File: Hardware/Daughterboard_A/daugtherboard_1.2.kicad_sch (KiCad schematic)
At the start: 66 parts, among them J2 RJ45, J3 RJ45, J4 Conn_01x07, J5 Conn_01x04, J6 Conn_01x07, U1 IM66D132H, U16 TXS0108EPW, U17 LP5907MFX-1.8/NOPB, U2 IM66D132H, U3 IM66D132H, U4 IM66D132H, U5 IM66D132H, U6 IM66D132H, U7 IM66D132H, U8 IM66D132H, U9 PCMD3180IRTWR

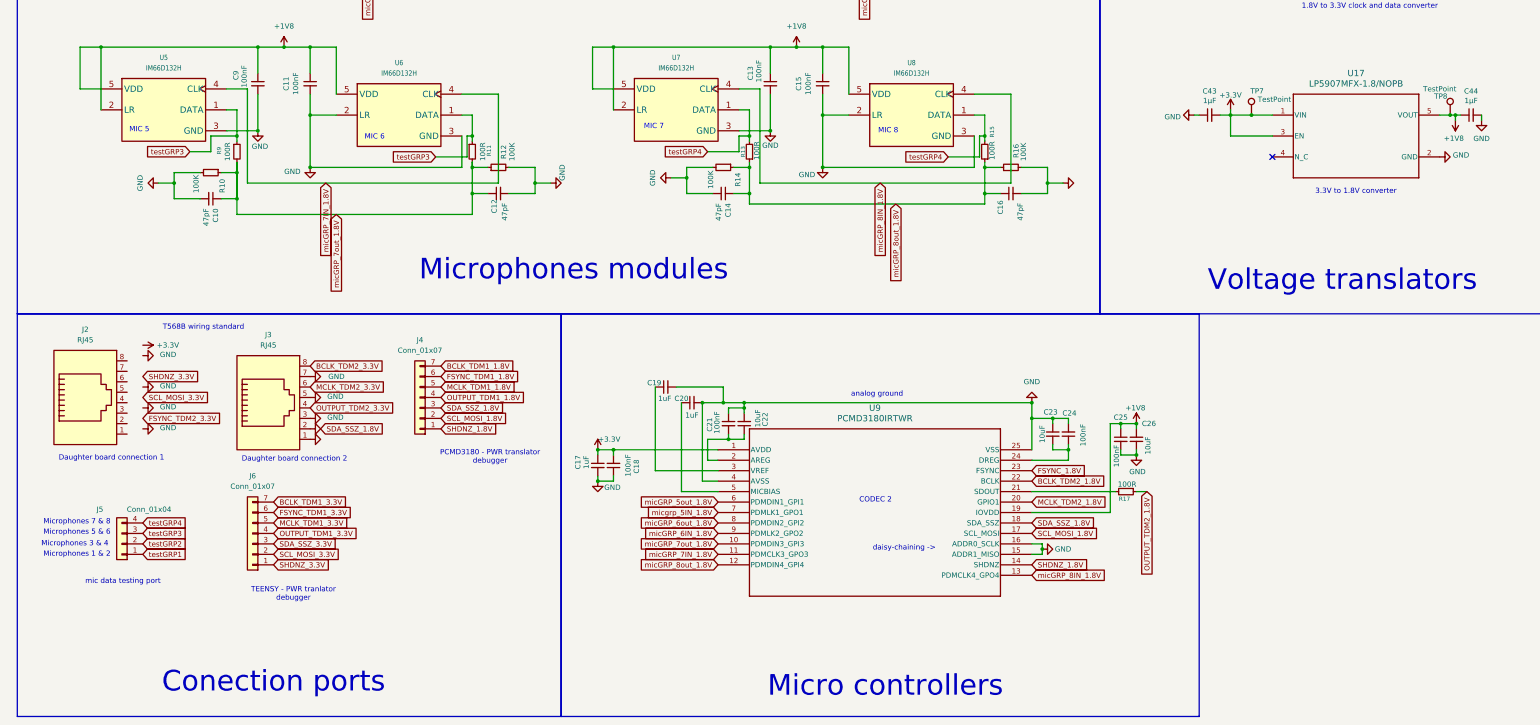
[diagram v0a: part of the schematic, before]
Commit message: ethernet port updated, fixed flaws 1.1 DB
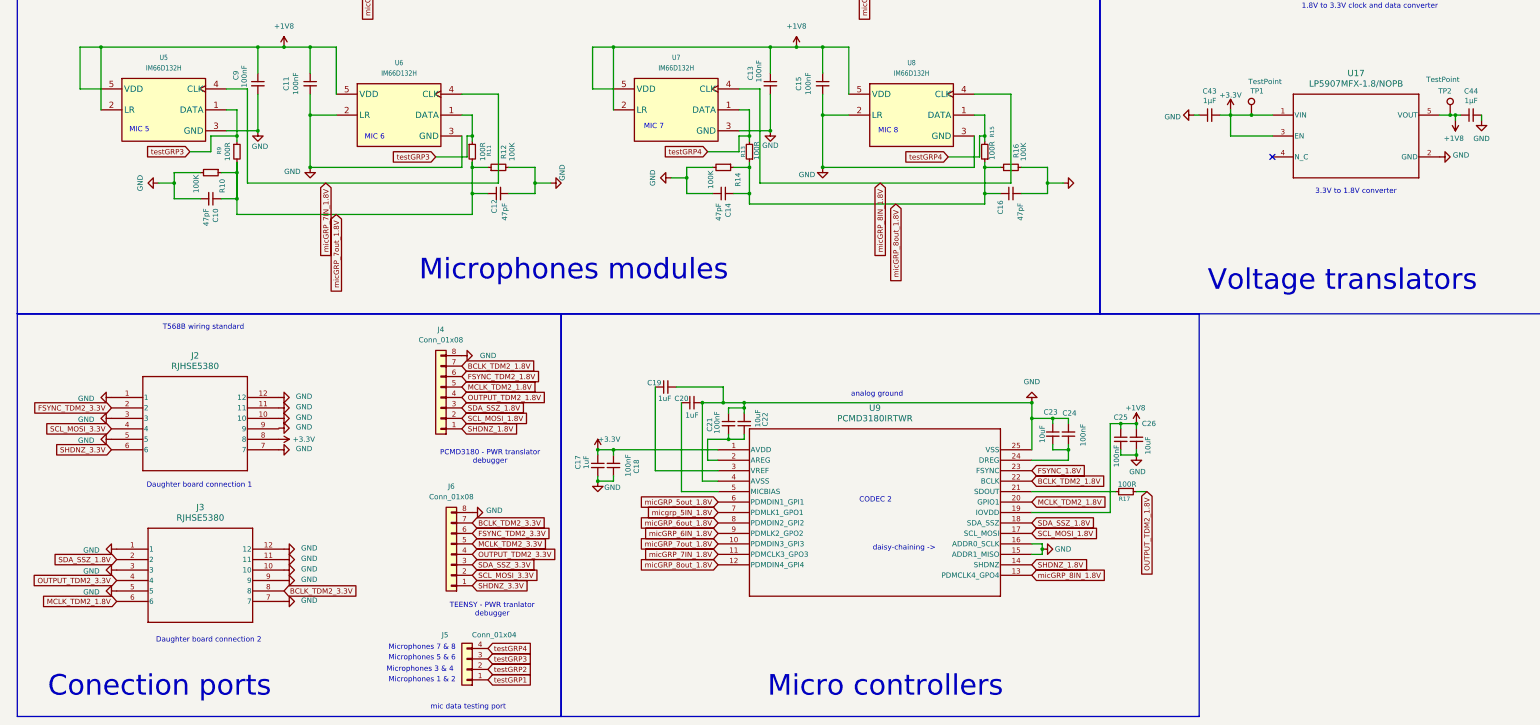
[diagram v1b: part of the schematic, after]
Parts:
- removed J2, J3: RJ45, RJHSE-3380:CONN_RJHSE-3380_AMP, symbol Connector:RJ45
- removed J4, J6: Conn_01x07, Connector_PinHeader_1.00mm:PinHeader_1x07_P1.00mm_Vertical, symbol Connector_Generic:Conn_01x07
- added J2, J3: RJHSE5380, RJHSE5380_AMP, symbol Ethernet R/A:RJHSE5380
- added J4, J6: Conn_01x08, symbol Connector_Generic:Conn_01x08
- renumbered TP7 to TP1, TP8 to TP2
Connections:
- net +3.3V: now also J2.8
- net BCLK_TDM2_1.8V: now also J4.7 (Pin_7)
- net BCLK_TDM2_3.3V: now also J3.8, J6.7 (Pin_7)
- net FSYNC_TDM2_1.8V: now also J4.6 (Pin_6)
- net FSYNC_TDM2_3.3V: now also J2.2, J6.6 (Pin_6)
- net GND: now also J2.1, J2.10, J2.11, J2.12, J2.3, J2.5, J2.7, J3.1, J3.10, J3.11, J3.12, J3.3, J3.5, J3.7, J3.9, J4.8 (Pin_8), J6.8 (Pin_8)
- net MCLK_TDM2_1.8V: now also J3.6, J4.5 (Pin_5)
- net MCLK_TDM2_3.3V: now also J6.5 (Pin_5)
- net OUTPUT_TDM2_1.8V: now also J4.4 (Pin_4)
- net OUTPUT_TDM2_3.3V: now also J3.4, J6.4 (Pin_4)
- net SCL_MOSI_1.8V: now also J4.2 (Pin_2)
- net SCL_MOSI_3.3V: now also J2.4, J6.2 (Pin_2)
- net SDA_SSZ_1.8V: now also J3.2, J4.3 (Pin_3)
- net SDA_SSZ_3.3V: now also J6.3 (Pin_3)
- net SHDNZ_1.8V: now also J4.1 (Pin_1)
- net SHDNZ_3.3V: now also J2.6, J6.1 (Pin_1)
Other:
- moved on the sheet: J5

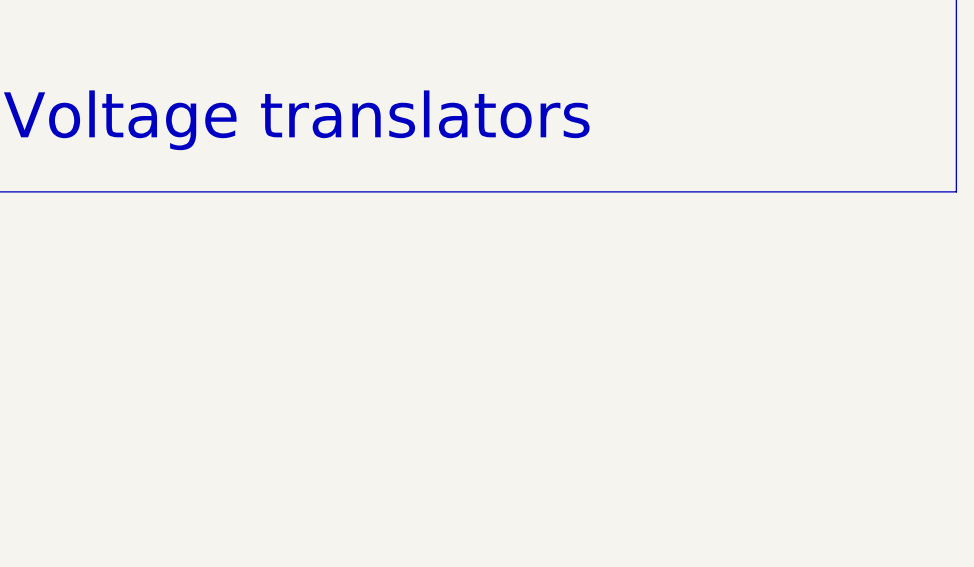
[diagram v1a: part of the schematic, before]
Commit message: implemented  ethernet port pcb R/a
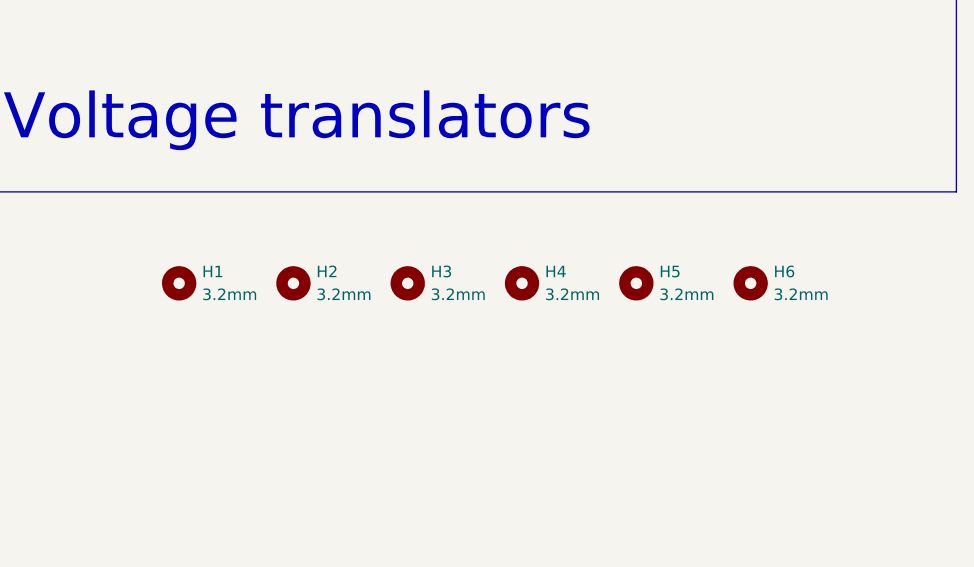
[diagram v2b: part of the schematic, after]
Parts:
- added H1, H2, H3, H4, H5, H6: 3.2mm, MountingHole:MountingHole_3.2mm_M3_ISO14580, symbol Mechanical:MountingHole
- J2, J3: footprint RJHSE5380_AMP -> RJHSE-5380:RJHSE5380_AMP
- J4, J6: footprint (none) -> Connector_PinHeader_2.00mm:PinHeader_1x08_P2.00mm_Vertical
- J5: footprint Connector_PinHeader_1.00mm:PinHeader_1x04_P1.00mm_Vertical -> Connector_PinHeader_2.00mm:PinHeader_1x04_P2.00mm_Vertical
